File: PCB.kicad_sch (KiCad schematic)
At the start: 35 parts, among them J1 USB_C_Receptacle_USB2.0_16P, SW1 SW_DIP_x02, SW2 SW_DIP_x02, SW3 SW_DIP_x02, U1 ESP32-S3-WROOM-1, U2 TMC2209_SILENTSTEPSTICK, U3 TMC2209_SILENTSTEPSTICK, U4 TMC2209_SILENTSTEPSTICK, U6 D3V3XA4B10LP, U7 AMS1117-3.3 (UMW)

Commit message: Ajout MD et correction erreurs
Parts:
- removed S1: BOOT, SKRKAEE020, symbol SKRKAEE020:SKRKAEE020
- removed S2: RST, SKRKAEE020, symbol SKRKAEE020:SKRKAEE020
- removed S3: BUILTIN, SKRKAEE020, symbol SKRKAEE020:SKRKAEE020
- added C1: 0.1uF(50V/10%), symbol Device:C
- added C7, C8: 10uF(25V/20%), symbol Device:C
- added J2: Conn_01x02_Pin, Connector_PinHeader_2.54mm:PinHeader_1x02_P2.54mm_Vertical, symbol Connector:Conn_01x02_Pin
- added SW4, SW5, SW6: SW_Push, Button_Switch_SMD:SW_Push_SPST_NO_Alps_SKRK, symbol Switch:SW_Push
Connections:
- net 3V3 is gone; now on net GND: C6.1, R3.1, U1.2 (3V3), U7.2 (VO)
- net ESP32_EN: now also C2.1, SW4.2
- net GND: now also C1.1, C1.2, C7.1, C7.2, C8.2, SW4.1, SW5.1, SW6.1
- net GPIO0: now also SW5.2
- net GPIOX: now also SW6.2; no longer BZ1.1 (+)
- net VCC_5V: now also C8.1
- net LED: now reaches U1.39 (IO1)
- net LED: now also D3.2 (A)
- net BUZZER: now reaches U1.4 (IO4)
- net BUZZER: now also BZ1.1 (+)
- no-connect marks 7 -> 13
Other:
- note added: "BAU"
- note added: "Boutons équipe"
- note added: "Tirette"
- moved on the sheet: C2, C3, C4, R3, TX0/RX0, TX1/RX1, U1

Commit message: Ajout empreintes
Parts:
- removed C4: 0.1uF, symbol Device:C
- removed D2: ~, Package_TO_SOT_THT:TO-18-2_Window, symbol LED:SFH482
- removed R5: 1000, symbol Device:R
- removed SW1, SW2, SW3: SW_DIP_x02, symbol Switch:SW_DIP_x02
- removed SW6: SW_Push, Button_Switch_SMD:SW_Push_SPST_NO_Alps_SKRK, symbol Switch:SW_Push
- removed TOF1, TOF2, TOF3: Conn_01x04_Pin, Connector_PinHeader_2.54mm:PinHeader_1x04_P2.54mm_Vertical, symbol Connector:Conn_01x04_Pin
- removed U3, U4: TMC2209_SILENTSTEPSTICK, TMC2209:MODULE_TMC2209_SILENTSTEPSTICK, symbol TMC2209_SILENTSTEPSTICK:TMC2209_SILENTSTEPSTICK
- added C3, C6, C8: 100uF, Capacitor_SMD:C_Elec_10x10.2, symbol Device:C
- added J2, J3, J4: Conn_01x04_Pin, Connector_PinHeader_2.54mm:PinHeader_1x04_P2.54mm_Vertical, symbol Connector:Conn_01x04_Pin
- added J5, J6: Conn_01x02_Pin, Connector_PinHeader_2.54mm:PinHeader_1x02_P2.54mm_Vertical, symbol Connector:Conn_01x02_Pin
- added JP1, JP2, JP3, JP4, JP5, JP6: Jumper_2_Open, TestPoint:TestPoint_2Pads_Pitch2.54mm_Drill0.8mm, symbol Jumper:Jumper_2_Open
- added TOF1, TOF2, TOF3: Conn_01x05_Pin, symbol Connector:Conn_01x05_Pin
- added U1, U5: TMC2209_SILENTSTEPSTICK, TMC2209:MODULE_TMC2209_SILENTSTEPSTICK, symbol TMC2209_SILENTSTEPSTICK:TMC2209_SILENTSTEPSTICK
- BZ1: footprint (none) -> Buzzer_Beeper:Buzzer_12x9.5RM7.6
- C1: renamed from C3; footprint (none) -> Resistor_SMD:R_01005_0402Metric
- C10: renamed from C1; footprint (none) -> Resistor_SMD:R_01005_0402Metric
- C2, R2: footprint (none) -> Resistor_SMD:R_01005_0402Metric
- C4: renamed from C8; footprint (none) -> Resistor_SMD:R_01005_0402Metric
- C5: footprint (none) -> Resistor_SMD:R_0603_1608Metric
- C7: renamed from C6; footprint (none) -> Resistor_SMD:R_0603_1608Metric
- C9: renamed from C7; footprint (none) -> Resistor_SMD:R_01005_0402Metric
- D1: footprint Package_TO_SOT_THT:TO-18-2_Window -> LED_SMD:LED_0603_1608Metric
- D2: renamed from D3; footprint Package_TO_SOT_THT:TO-18-2_Window -> LED_SMD:LED_0603_1608Metric
- R1: renamed from R3; footprint (none) -> Resistor_SMD:R_01005_0402Metric
- R3: renamed from R1; footprint (none) -> Resistor_SMD:R_01005_0402Metric
- R4: value 1000 -> 120; footprint (none) -> Resistor_SMD:R_01005_0402Metric
- R5: renamed from R6; value 1000 -> 120; footprint (none) -> Resistor_SMD:R_01005_0402Metric
- renumbered J2 to J7, SW5 to SW1, SW4 to SW2, TX0/RX0 to TX0/RX1, U6 to U3, U7 to U4, U1 to U6
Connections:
- net GND: now also D1.2 (A), J7.2 (Pin_2), U2.16 (~{EN}), C3.2, C6.2, C8.2, J5.2 (Pin_2), TOF1.4 (Pin_4), TOF2.4 (Pin_4), TOF3.4 (Pin_4), U1.1 (GND), U1.16 (~{EN}), U1.7 (GND), U5.1 (GND), U5.16 (~{EN}), U5.7 (GND)
- net LED: now also U6.5 (IO5); no longer U6.39 (IO1)
- net SCL: now also TOF1.3 (Pin_3), TOF2.3 (Pin_3), TOF3.3 (Pin_3)
- net SDA: now also U6.39 (IO1), TOF1.2 (Pin_2), TOF2.2 (Pin_2), TOF3.2 (Pin_2); no longer U6.15 (IO3)
- net VCC_5V: now also U2.2 (VIO), U2.8 (VM), C3.1, C6.1, C8.1, J6.1 (Pin_1), JP1.1 (A), JP2.1 (A), JP3.1 (A), JP4.1 (A), JP5.1 (A), JP6.1 (A), TOF1.5 (Pin_5), TOF2.5 (Pin_5), TOF3.5 (Pin_5), U1.2 (VIO), U1.8 (VM), U5.2 (VIO), U5.8 (VM); no longer D1.2 (A), J1.A4 (VBUS), J1.A9 (VBUS), J1.B4 (VBUS), J1.B9 (VBUS)
- net at U2.14 (MS2): now also JP4.2 (B)
- net at U2.15 (MS1): now also JP3.2 (B)
- net XSHUT1: now reaches U6.12 (IO8)
- net XSHUT1: now also TOF1.1 (Pin_1)
- net XSHUT2: now reaches U6.17 (IO9)
- net XSHUT2: now also TOF2.1 (Pin_1)
- net XSHUT3: now reaches U6.18 (IO10)
- net XSHUT3: now also TOF3.1 (Pin_1)
- net STEP1: now reaches U6.19 (IO11)
- net STEP1: now also U1.10 (STEP)
- net STEP2: now reaches U6.20 (IO12)
- net STEP2: now also U2.10 (STEP)
- net STEP3: now reaches U6.21 (IO13)
- net STEP3: now also U5.10 (STEP)
- net DIR1: now reaches U6.22 (IO14)
- net DIR1: now also U1.9 (DIR)
- net GPIO21: now reaches U6.23 (IO21)
- net GPIO47: now reaches U6.24 (IO47)
- net GPIO48: now reaches U6.25 (IO48)
- net GPIO35: now reaches U6.28 (IO35)
- net GPIO36: now reaches U6.29 (IO36)
- net GPIO37: now reaches U6.30 (IO37)
- net GPIO38: now reaches U6.31 (IO38)
- net LAUNCHPULL: now reaches U6.6 (IO6)
- net LAUNCHPULL: now also J7.1 (Pin_1)
- net TEAMBTN: now reaches U6.7 (IO7)
- net TEAMBTN: now also J5.1 (Pin_1)
- net DIR2: now reaches U6.8 (IO15)
- net DIR2: now also U2.9 (DIR)
- net DIR3: now reaches U6.9 (IO16)
- net DIR3: now also U5.9 (DIR)
- net at U2.3 (M1B): now also J3.2 (Pin_2)
- net at U2.4 (M1A): now also J3.4 (Pin_4)
- net at U2.5 (M2A): now also J3.3 (Pin_3)
- net at U2.6 (M2B): now also J3.1 (Pin_1)
- new net: JP5.2 (B), U5.15 (MS1)
- new net: JP2.2 (B), U1.14 (MS2)
- new net: JP1.2 (B), U1.15 (MS1)
- new net: J2.2 (Pin_2), U1.3 (M1B)
- new net: J2.4 (Pin_4), U1.4 (M1A)
- new net: J2.3 (Pin_3), U1.5 (M2A)
- new net: J2.1 (Pin_1), U1.6 (M2B)
- new net: J4.1 (Pin_1), U5.6 (M2B)
- new net: J4.2 (Pin_2), U5.3 (M1B)
- new net: J4.3 (Pin_3), U5.5 (M2A)
- new net: J4.4 (Pin_4), U5.4 (M1A)
- new net: JP6.2 (B), U5.14 (MS2)
- new net VCC_5Vin: J1.A4 (VBUS), J1.A9 (VBUS), J1.B4 (VBUS), J1.B9 (VBUS), J6.2 (Pin_2)
- no-connect marks 13 -> 11
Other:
- note added: "- BOOT Button - RESET Button"
- note added: "3x TMC2209 Drivers to control 3x NEMA 17 with 1A/phase each +Jumper to control step"
- note added: "Buttons"
- note added: "ESP32-S3-1 (No PSRAM)"
- note added: "LEDs"
- note added: "Launch pull"
- note added: "M1 = Phase M2 = Phase"
- note added: "ORANGE = GPIOX"
- note added: "Pull-down when open"
- note added: "Team button"
- note added: "VCC_5Vin -> BAU -> VCC_5V"
- note removed: "- BOOT Button - RESET Button - BUILTIN Button"
- note removed: "3x TMC2209 Drivers to control 3x NEMA 17 with 1A/phase each +Switch to control step"
- note removed: "Boutons équipe"
- note removed: "Buttons x3"
- note removed: "ESP32-S3-U1"
- note removed: "Flash LED"
- note removed: "LEDs x3"
- note removed: "ORANGE = Working on"
- note removed: "Tirette"
- moved on the sheet: C1, C2, C5, C7, D1, D2, R1, R2, R3, R4, R5, SCREEN1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

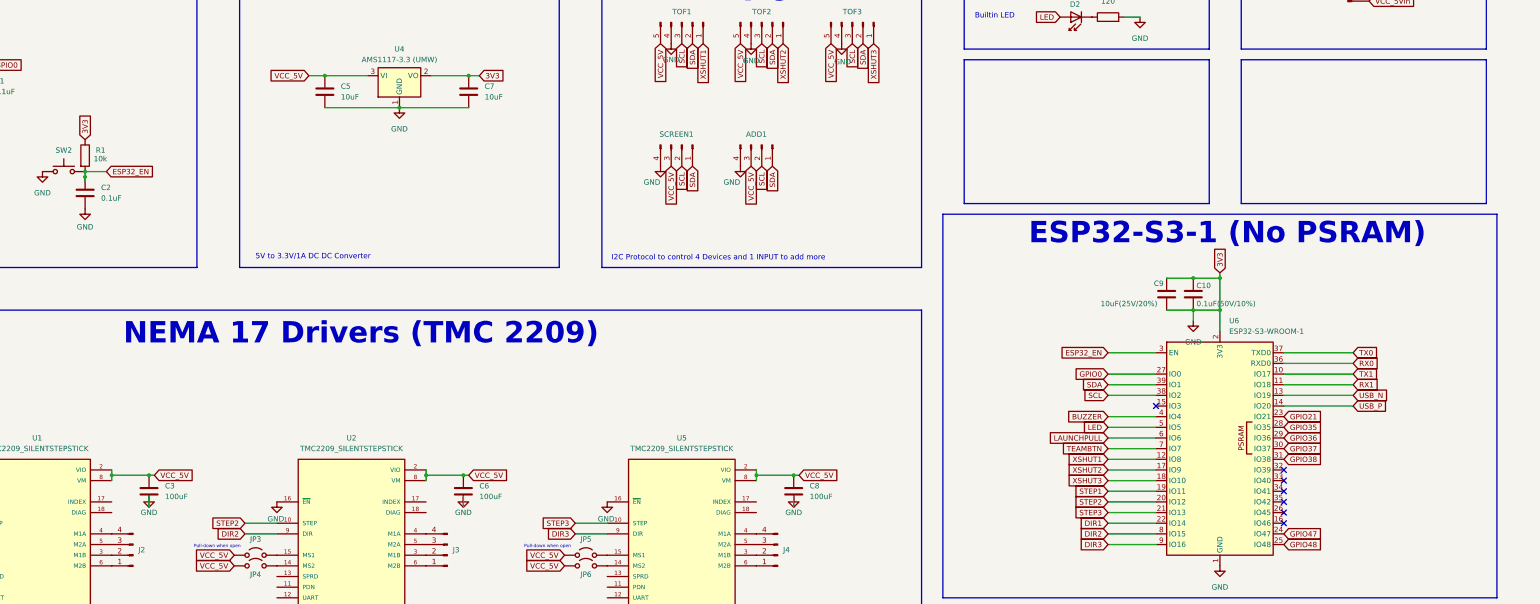
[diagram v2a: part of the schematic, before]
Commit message: Fix court-circuit
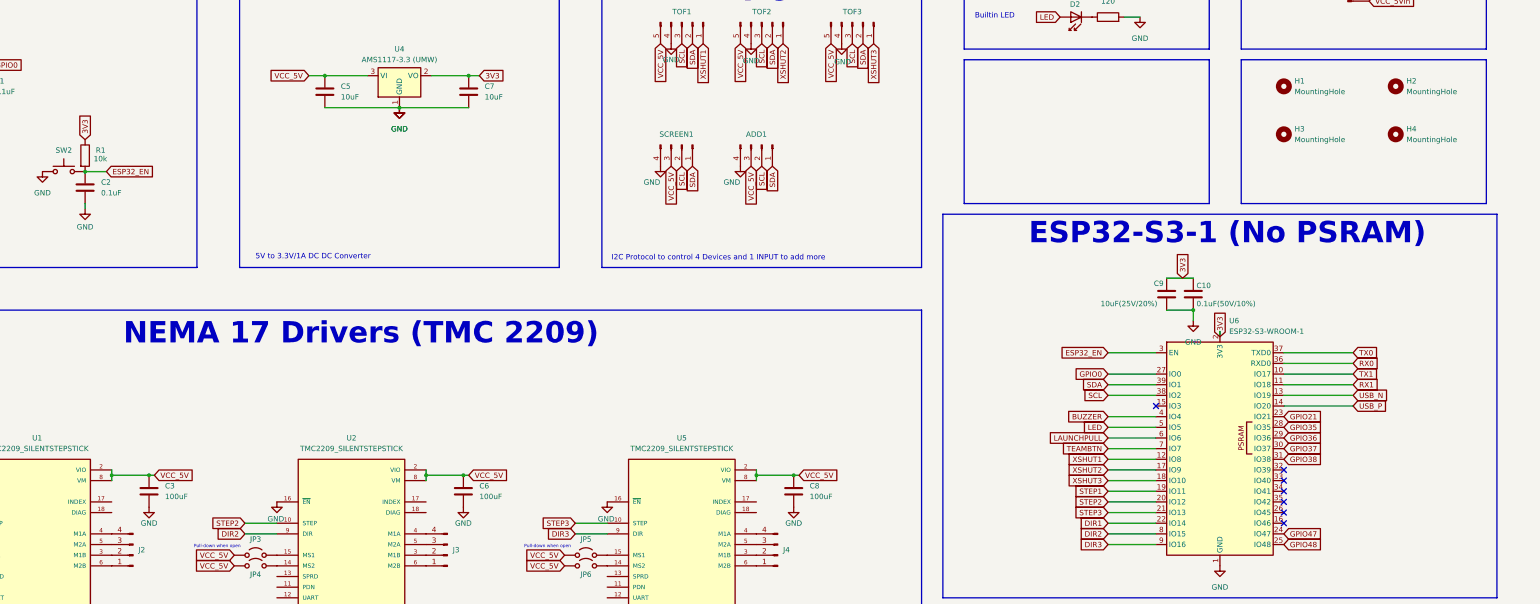
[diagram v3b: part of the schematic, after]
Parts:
- added H1, H2, H3, H4: MountingHole, MountingHole:MountingHole_3.2mm_M3, symbol Mechanical:MountingHole
- TOF1, TOF2, TOF3: footprint (none) -> Connector_PinHeader_2.54mm:PinHeader_1x05_P2.54mm_Vertical
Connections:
- net GND: no longer C10.1, C7.1, C9.1, D1.2 (A), R1.1, U4.2 (VO), U6.2 (3V3)
- new net 3V3: C10.1, C7.1, C9.1, D1.2 (A), R1.1, U4.2 (VO), U6.2 (3V3)
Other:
- moved on the sheet: C2

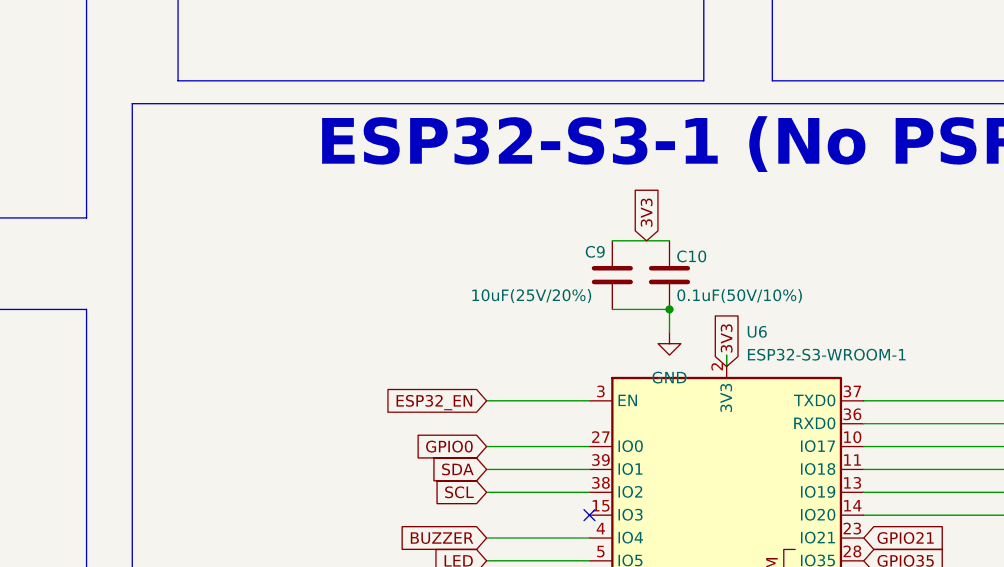
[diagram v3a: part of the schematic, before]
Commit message: Correction bug schématic
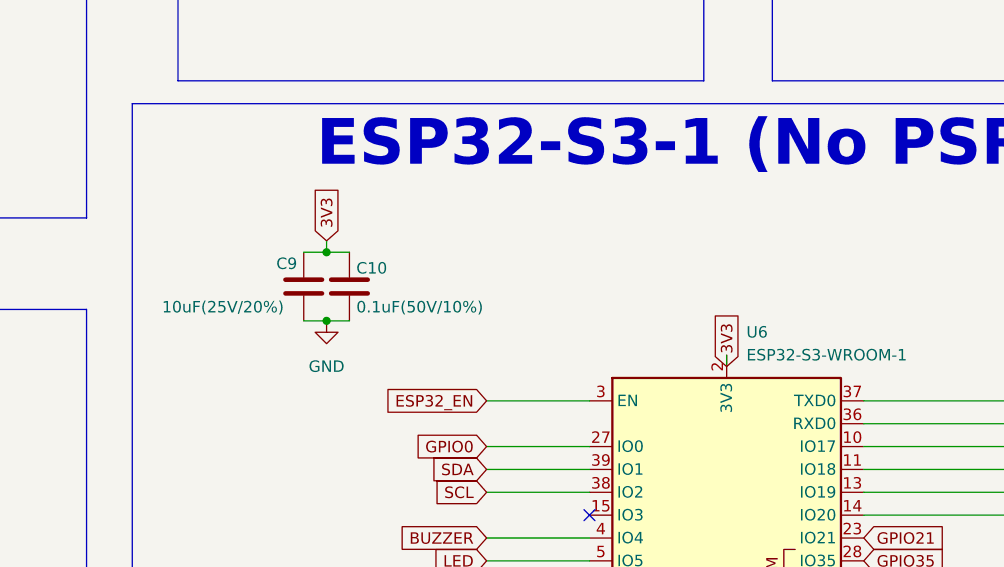
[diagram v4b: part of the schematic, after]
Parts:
- C3, C6, C8: footprint Capacitor_SMD:C_Elec_10x10.2 -> Capacitor_THT:CP_Radial_D10.0mm_P5.00mm
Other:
- moved on the sheet: C10, C9
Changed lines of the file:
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@@
 	)
 	(junction
+		(at 290.83 176.53)
+		(diameter 0)
+		(color 0 0 0 0)
+	)
+	(junction
 		(at 48.26 80.01)
 		(diameter 0)
@@
 	)
 	(junction
-		(at 154.94 222.25)
+		(at 290.83 184.15)
 		(diameter 0)
 		(color 0 0 0 0)
 	)
 	(junction
-		(at 328.93 182.88)
+		(at 154.94 222.25)
 		(diameter 0)
 		(color 0 0 0 0)
@@
 	(wire
 		(pts
-			(xy 322.58 182.88) (xy 328.93 182.88)
+			(xy 288.29 184.15) (xy 290.83 184.15)
 		)
 		(stroke
@@
 	(wire
 		(pts
+			(xy 290.83 175.26) (xy 290.83 176.53)
+		)
+		(stroke
+			(width 0)
+			(type default)
+		)
+	)
+	(wire
+		(pts
 			(xy 63.5 59.69) (xy 63.5 62.23)
 		)
@@
 	(wire
 		(pts
+			(xy 290.83 176.53) (xy 293.37 176.53)
+		)
+		(stroke
+			(width 0)
+			(type default)
+		)
+	)
+	(wire
+		(pts
 			(xy 308.61 233.68) (xy 320.04 233.68)
 		)
@@
 	(wire
 		(pts
-			(xy 328.93 182.88) (xy 328.93 185.42)
-		)
-		(stroke
-			(width 0)
-			(type default)
-		)
-	)
-	(wire
-		(pts
 			(xy 71.12 220.98) (xy 71.12 222.25)
 		)
@@
 	(wire
 		(pts
-			(xy 322.58 175.26) (xy 328.93 175.26)
+			(xy 288.29 176.53) (xy 290.83 176.53)
 		)
 		(stroke
@@
 	(wire
 		(pts
+			(xy 290.83 184.15) (xy 293.37 184.15)
+		)
+		(stroke
+			(width 0)
+			(type default)
+		)
+	)
+	(wire
+		(pts
 			(xy 224.79 220.98) (xy 224.79 222.25)
 		)
@@
 	(global_label "3V3"
 		(shape input)
-		(at 326.39 175.26 90)
+		(at 290.83 175.26 90)
 		(fields_autoplaced yes)
 		(effects
@@
 		)
 		(property "Intersheetrefs" "${INTERSHEET_REFS}"
-			(at 326.39 168.7672 90)
+			(at 290.83 168.7672 90)
 			(effects
 				(font
@@
 			)
 		)
-		(property "Footprint" "Capacitor_SMD:C_Elec_10x10.2"
+		(property "Footprint" "Capacitor_THT:CP_Radial_D10.0mm_P5.00mm"
 			(at 234.6452 229.87 0)
 			(effects
@@
 	(symbol
 		(lib_id "Device:C")
-		(at 328.93 179.07 0)
+		(at 293.37 180.34 0)
 		(unit 1)
 		(exclude_from_sim no)
@@
 		(dnp no)
 		(property "Reference" "C10"
-			(at 329.692 177.038 0)
+			(at 294.132 178.308 0)
 			(effects
 				(font
@@
 		)
 		(property "Value" "0.1uF(50V/10%)"
-			(at 329.692 181.356 0)
+			(at 294.132 182.626 0)
 			(effects
 				(font
@@
 		)
 		(property "Footprint" "Resistor_SMD:R_01005_0402Metric"
-			(at 329.8952 182.88 0)
+			(at 294.3352 184.15 0)
 			(effects
 				(font
@@
 		)
 		(property "Datasheet" "~"
-			(at 328.93 179.07 0)
+			(at 293.37 180.34 0)
 			(effects
 				(font
@@
 		)
 		(property "Description" "Unpolarized capacitor"
-			(at 328.93 179.07 0)
+			(at 293.37 180.34 0)
 			(effects
 				(font
@@
 			)
 		)
-		(property "Footprint" "Capacitor_SMD:C_Elec_10x10.2"
+		(property "Footprint" "Capacitor_THT:CP_Radial_D10.0mm_P5.00mm"
 			(at 80.9752 229.87 0)
 			(effects
@@
 	(symbol
 		(lib_id "Device:C")
-		(at 322.58 179.07 0)
+		(at 288.29 180.34 0)
 		(unit 1)
 		(exclude_from_sim no)
@@
 		(dnp no)
 		(property "Reference" "C9"
-			(at 319.532 176.53 0)
+			(at 285.242 177.8 0)
 			(effects
 				(font
@@
 		)
 		(property "Value" "10uF(25V/20%)"
-			(at 306.832 181.356 0)
+			(at 272.542 182.626 0)
 			(effects
 				(font
@@
 		)
 		(property "Footprint" "Resistor_SMD:R_01005_0402Metric"
-			(at 323.5452 182.88 0)
+			(at 289.2552 184.15 0)
 			(effects
 				(font
@@
 		)
 		(property "Datasheet" "~"
-			(at 322.58 179.07 0)
+			(at 288.29 180.34 0)
 			(effects
 				(font
@@
 		)
 		(property "Description" "Unpolarized capacitor"
-			(at 322.58 179.07 0)
+			(at 288.29 180.34 0)
 			(effects
 				(font
@@
 			)
 		)
-		(property "Footprint" "Capacitor_SMD:C_Elec_10x10.2"
+		(property "Footprint" "Capacitor_THT:CP_Radial_D10.0mm_P5.00mm"
 			(at 155.9052 229.87 0)
 			(effects
@@
 	(symbol
 		(lib_id "power:GND")
-		(at 328.93 185.42 0)
+		(at 290.83 184.15 0)
 		(unit 1)
 		(exclude_from_sim no)
@@
 		(fields_autoplaced yes)
 		(property "Reference" "#PWR029"
-			(at 328.93 191.77 0)
+			(at 290.83 190.5 0)
 			(effects
 				(font
@@
 		)
 		(property "Value" "GND"
-			(at 328.93 190.5 0)
+			(at 290.83 189.23 0)
 			(effects
 				(font
@@
 		)
 		(property "Footprint" ""
-			(at 328.93 185.42 0)
+			(at 290.83 184.15 0)
 			(effects
 				(font
@@
 		)
 		(property "Datasheet" ""
-			(at 328.93 185.42 0)
+			(at 290.83 184.15 0)
 			(effects
 				(font
@@
 		)
 		(property "Description" "Power symbol creates a global label with name \"GND\" , ground"
-			(at 328.93 185.42 0)
+			(at 290.83 184.15 0)
 			(effects
 				(font

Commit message: routage terminé
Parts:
- removed J4: Conn_01x04_Pin, Connector_PinHeader_2.54mm:PinHeader_1x04_P2.54mm_Vertical, symbol Connector:Conn_01x04_Pin
- added J8: Conn_01x04_Pin, Connector_PinHeader_2.54mm:PinHeader_1x04_P2.54mm_Vertical, symbol Connector:Conn_01x04_Pin
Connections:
- net BUZZER: now also U6.5 (IO5); no longer U6.4 (IO4)
- net DIR2: now also U6.9 (IO16); no longer U6.8 (IO15)
- net DIR3: now also U6.8 (IO15); no longer U6.9 (IO16)
- net LED: now also U6.4 (IO4); no longer U6.5 (IO5)
- net STEP1: now also U6.21 (IO13); no longer U6.19 (IO11)
- net STEP3: now also U6.19 (IO11); no longer U6.21 (IO13)
- net MOTORA1: now reaches U1.3 (M1B)
- net MOTORA1: now also J8.1 (Pin_1); no longer J2.2 (Pin_2)
- net MOTORA2: now reaches U1.4 (M1A)
- net MOTORA2: now also J8.2 (Pin_2); no longer J2.4 (Pin_4)
- net MOTORA3: now reaches U1.5 (M2A)
- net MOTORA3: now also J8.3 (Pin_3); no longer J2.3 (Pin_3)
- net MOTORA4: now reaches U1.6 (M2B)
- net MOTORA4: now also J8.4 (Pin_4); no longer J2.1 (Pin_1)
- net MOTORC4: now reaches U5.6 (M2B)
- net MOTORC4: now also J3.4 (Pin_4)
- net MOTORC1: now reaches U5.3 (M1B)
- net MOTORC1: now also J3.1 (Pin_1)
- net MOTORC3: now reaches U5.5 (M2A)
- net MOTORC3: now also J3.3 (Pin_3)
- net MOTORC2: now reaches U5.4 (M1A)
- net MOTORC2: now also J3.2 (Pin_2)
- net MOTORB1: now reaches U2.3 (M1B)
- net MOTORB1: now also J2.1 (Pin_1); no longer J3.2 (Pin_2)
- net MOTORB2: now reaches U2.4 (M1A)
- net MOTORB2: now also J2.2 (Pin_2); no longer J3.4 (Pin_4)
- net MOTORB3: now reaches U2.5 (M2A)
- net MOTORB3: now also J2.3 (Pin_3); no longer J3.3 (Pin_3)
- net MOTORB4: now reaches U2.6 (M2B)
- net MOTORB4: now also J2.4 (Pin_4); no longer J3.1 (Pin_1)
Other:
- note added: "Mounting Holes"
- moved on the sheet: BZ1, D1, D2, H1, H2, H3, H4, R4, R5

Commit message: chnagement jumper + orga
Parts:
- added J4: Conn_01x07_Pin, Connector_PinHeader_2.54mm:PinHeader_1x04_P2.54mm_Vertical, symbol Connector:Conn_01x04_Pin
- added J9: Conn_01x07_Pin, Connector_PinHeader_2.54mm:PinHeader_1x03_P2.54mm_Vertical, symbol Connector:Conn_01x03_Pin
- JP1, JP2, JP3, JP4, JP5, JP6: footprint TestPoint:TestPoint_2Pads_Pitch2.54mm_Drill0.8mm -> Connector_PinHeader_2.54mm:PinHeader_1x02_P2.54mm_Vertical
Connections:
- net GPIO21: now also J9.1 (Pin_1)
- net GPIO35: now also J9.2 (Pin_2)
- net GPIO36: now also J4.1 (Pin_1)
- net GPIO37: now also J4.2 (Pin_2)
- net GPIO38: now also J4.3 (Pin_3)
- net GPIO47: now also J4.4 (Pin_4)
- net GPIO48: now also J9.3 (Pin_3)
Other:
- note added: "Unused GPIOs"

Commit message: ajout plus de 5V et GND
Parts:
- added J10, J11: Conn_01x05_Pin, Connector_PinHeader_2.54mm:PinHeader_1x05_P2.54mm_Vertical, symbol Connector:Conn_01x05_Pin
- added JP7, JP8: Jumper_2_Open, Resistor_SMD:R_1206_3216Metric_Pad1.30x1.75mm_HandSolder, symbol Jumper:Jumper_2_Open
- renumbered TX0/RX1 to UART0, TX1/RX1 to UART1
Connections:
- net GND: now also J11.1 (Pin_1), J11.2 (Pin_2), J11.3 (Pin_3), J11.4 (Pin_4), J11.5 (Pin_5)
- net SCL: now also JP7.2 (B)
- net SDA: now also JP8.2 (B)
- net VCC_5V: now also J10.1 (Pin_1), J10.2 (Pin_2), J10.3 (Pin_3), J10.4 (Pin_4), J10.5 (Pin_5), JP7.1 (A), JP8.1 (A)
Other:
- note added: "Add more 5V and GND pins to plug new modules"
- note added: "Can be used in input/output"
- note added: "More 5V & GND"
- note added: "Pull-up Resistors"
- note added: "Pull-up resistors location for modularity"
